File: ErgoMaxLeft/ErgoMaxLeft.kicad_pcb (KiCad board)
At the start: 2 copper layers, 182.8 x 178.9 mm, 94 parts, among them J1 AudioJack4_Ground, K1 KEYSW, K10 KEYSW, K11 KEYSW, K12 KEYSW, K13 KEYSW, K14 KEYSW, K15 KEYSW, K16 KEYSW, K17 KEYSW, K18 KEYSW, K19 KEYSW, K2 KEYSW, K20 KEYSW, K21 KEYSW, K22 KEYSW, K23 KEYSW, K24 KEYSW, K25 KEYSW, K26 KEYSW, K27 KEYSW, K28 KEYSW, K29 KEYSW, K3 KEYSW, K30 KEYSW, K31 KEYSW, K32 KEYSW, K33 KEYSW, K34 KEYSW, K35 KEYSW, K36 KEYSW, K37 KEYSW, K38 KEYSW, K39 KEYSW, K4 KEYSW, K40 KEYSW, K41 KEYSW, K42 KEYSW, K43 KEYSW, K44 KEYSW, K5 KEYSW, K6 KEYSW, K7 KEYSW, K8 KEYSW, K9 KEYSW, U1 ProMicro

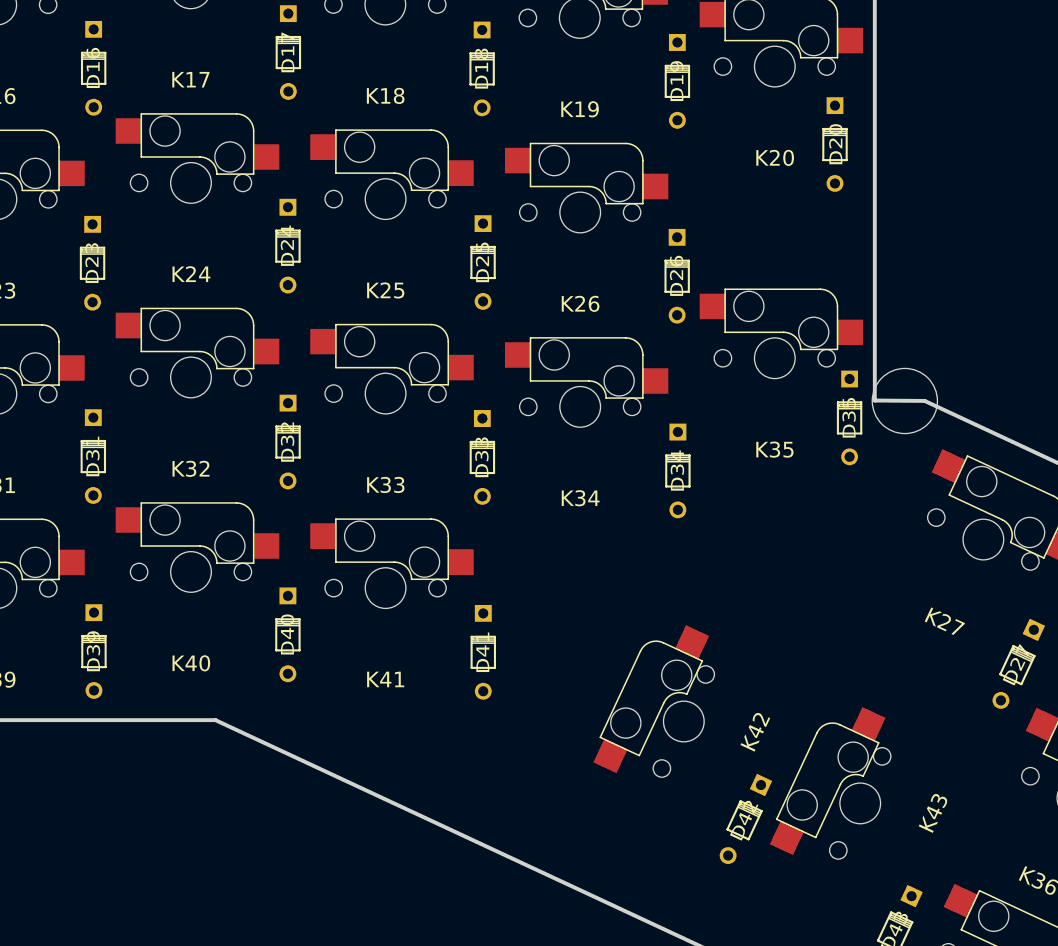
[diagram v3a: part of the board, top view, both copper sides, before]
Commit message: WIP PCB - add more mouting holes based on ErgoDox
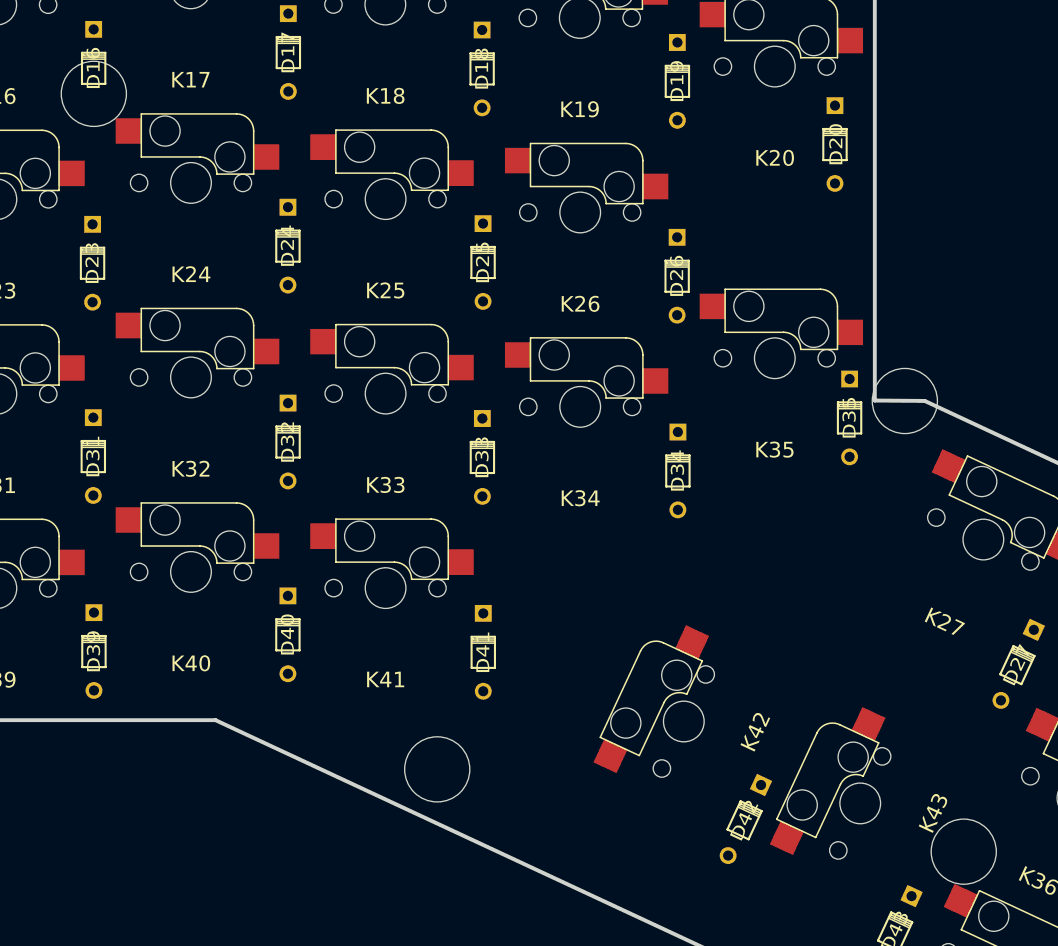
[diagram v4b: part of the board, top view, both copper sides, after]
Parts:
- added ?: , MountingHole:MountingHole_6.5mm_Pad, F.Cu at (177.2, 107.3)
- added ?: , MountingHole:MountingHole_6.5mm_Pad, F.Cu at (262.4, 181.5)
- added ?: , MountingHole:MountingHole_6.5mm_Pad, F.Cu at (210.8, 173.4)
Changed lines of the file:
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@@
     (tracks 0)
     (zones 0)
-    (modules 94)
+    (modules 97)
     (nets 67)
   )
@@
     (add_net VCC)
   )
+  (module MountingHole:MountingHole_6.5mm_Pad (layer F.Cu)
+    (at 177.200212 107.268092)
+    (descr "Mounting Hole 6.5mm")
+    (tags "mounting hole 6.5mm")
+    (attr virtual)
+    (fp_text reference "" (at 0 -7.5) (layer F.SilkS) hide
+      (effects (font (size 1 1) (thickness 0.15)))
+    )
+    (fp_text value "" (at 0 7.5) (layer F.Fab) hide
+      (effects (font (size 1 1) (thickness 0.15)))
+    )
+    (fp_text user %R (at 0.3 0) (layer F.Fab)
+      (effects (font (size 1 1) (thickness 0.15)))
+    )
+    (fp_circle (center 0 0) (end 6.5 0) (layer Cmts.User) (width 0.15))
+    (fp_circle (center 0 0) (end 6.75 0) (layer F.CrtYd) (width 0.05))
+    (pad "" np_thru_hole circle (at 0 0) (size 6.3754 6.3754) (drill 6.3754) (layers *.Cu *.Mask)
+      (solder_mask_margin -0.254))
+  )
+  (module MountingHole:MountingHole_6.5mm_Pad (layer F.Cu)
+    (at 262.355601 181.45146)
+    (descr "Mounting Hole 6.5mm")
+    (tags "mounting hole 6.5mm")
+    (attr virtual)
+    (fp_text reference "" (at 0 -7.5) (layer F.SilkS) hide
+      (effects (font (size 1 1) (thickness 0.15)))
+    )
+    (fp_text value "" (at 0 7.5) (layer F.Fab) hide
+      (effects (font (size 1 1) (thickness 0.15)))
+    )
+    (fp_text user %R (at 0.3 0) (layer F.Fab)
+      (effects (font (size 1 1) (thickness 0.15)))
+    )
+    (fp_circle (center 0 0) (end 6.5 0) (layer Cmts.User) (width 0.15))
+    (fp_circle (center 0 0) (end 6.75 0) (layer F.CrtYd) (width 0.05))
+    (pad "" np_thru_hole circle (at 0 0) (size 6.3754 6.3754) (drill 6.3754) (layers *.Cu *.Mask)
+      (solder_mask_margin -0.254))
+  )
+  (module MountingHole:MountingHole_6.5mm_Pad (layer F.Cu)
+    (at 210.814547 173.394127)
+    (descr "Mounting Hole 6.5mm")
+    (tags "mounting hole 6.5mm")
+    (attr virtual)
+    (fp_text reference "" (at 0 -7.5) (layer F.SilkS) hide
+      (effects (font (size 1 1) (thickness 0.15)))
+    )
+    (fp_text value "" (at 0 7.5) (layer F.Fab) hide
+      (effects (font (size 1 1) (thickness 0.15)))
+    )
+    (fp_text user %R (at 0.3 0) (layer F.Fab)
+      (effects (font (size 1 1) (thickness 0.15)))
+    )
+    (fp_circle (center 0 0) (end 6.5 0) (layer Cmts.User) (width 0.15))
+    (fp_circle (center 0 0) (end 6.75 0) (layer F.CrtYd) (width 0.05))
+    (pad "" np_thru_hole circle (at 0 0) (size 6.3754 6.3754) (drill 6.3754) (layers *.Cu *.Mask)
+      (solder_mask_margin -0.254))
+  )
   (module MountingHole:MountingHole_6.4mm_M6 (layer F.Cu)

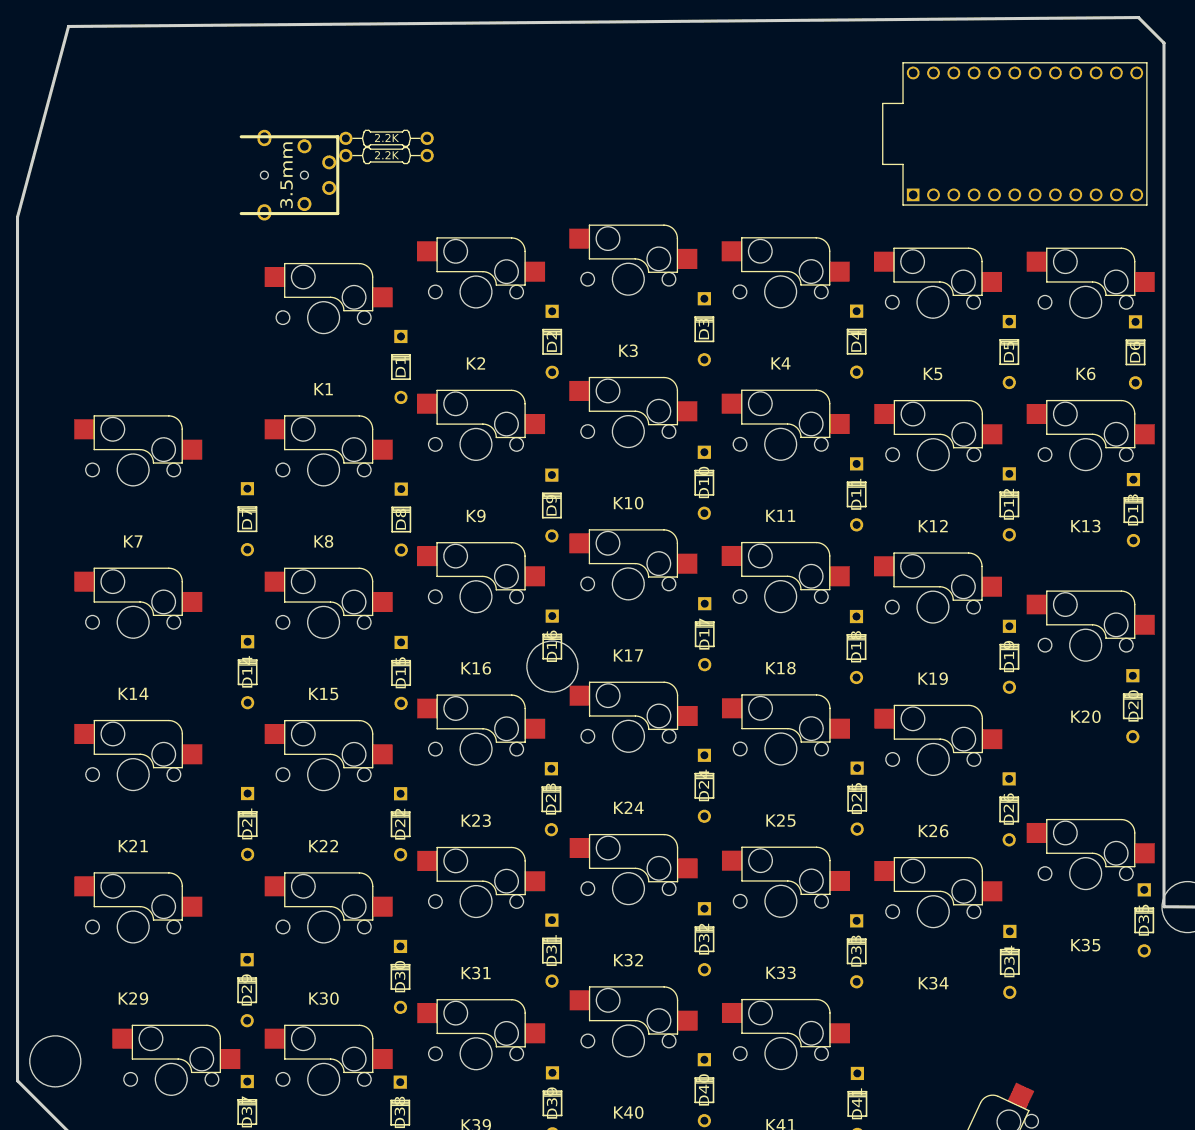
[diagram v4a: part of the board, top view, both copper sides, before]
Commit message: WIP PCB - make proper cutout for the top
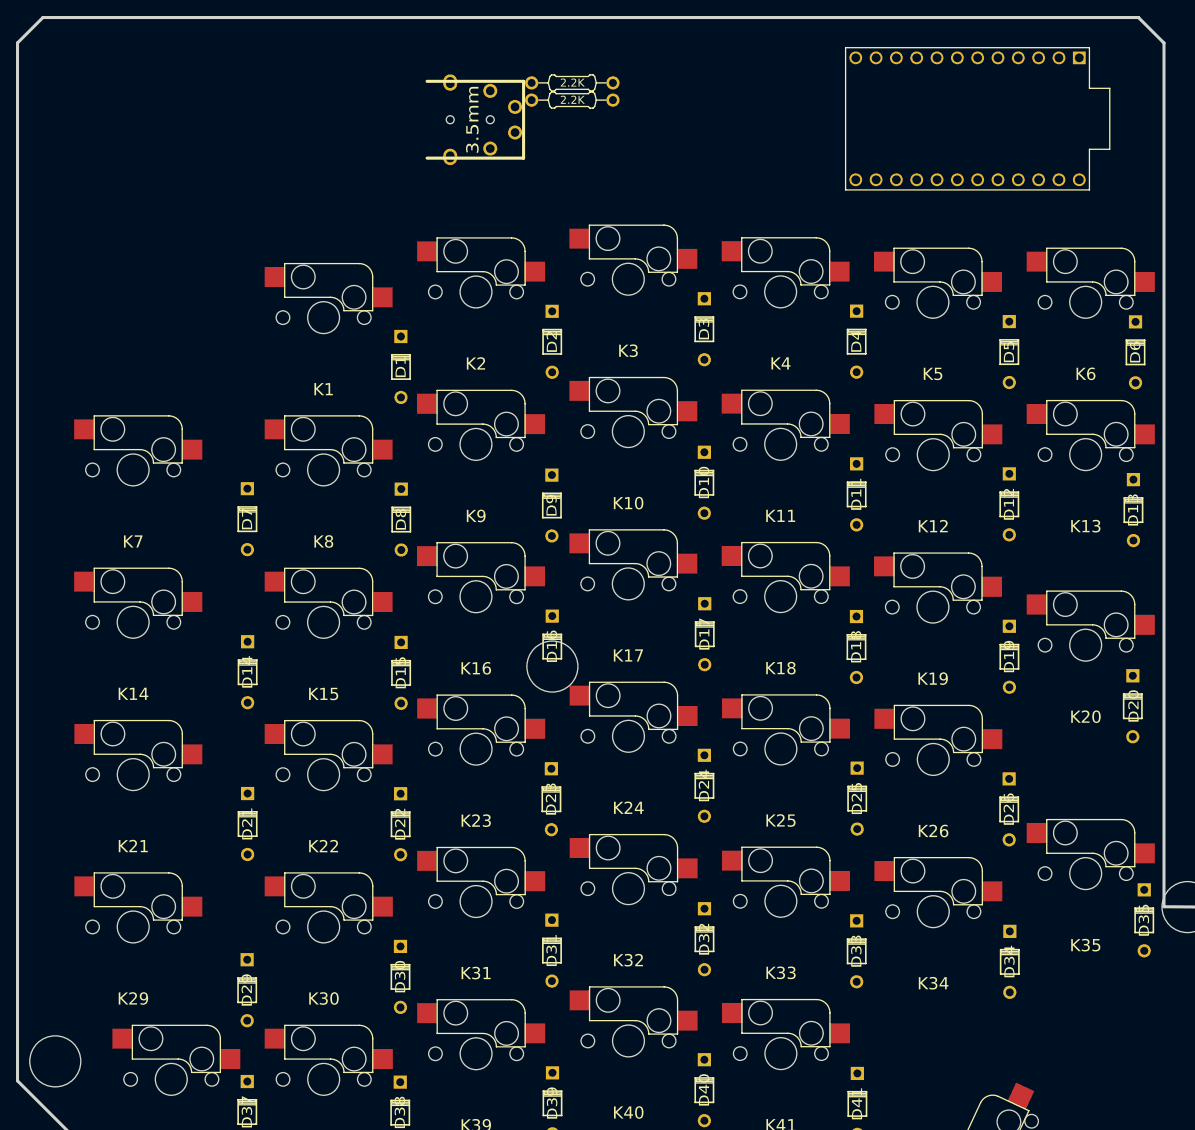
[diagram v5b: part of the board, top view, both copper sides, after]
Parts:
- moved J1 24.2 mm to (161.5, 38.9)
- moved R1 24.2 mm to (179.7, 36.5)
- moved R2 24.2 mm to (179.7, 34.3)
- moved U1 7.42 mm to (229.1, 38.8), turned to 180 degrees
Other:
- outline, holes or cut-outs redrawn
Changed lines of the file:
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@@
   )
   (module Keebio-Parts:4pin35mmAudio (layer F.Cu)
-    (at 138.30298 45.84516)
+    (at 161.53298 38.91516)
     (fp_text reference J1 (at 1.27 0 90) (layer F.SilkS) hide
       (effects (font (size 1.524 1.778) (thickness 0.3048)))
@@
   )
   (module Keebio-Parts:Resistor (layer F.Cu)
-    (at 156.45848 43.393261)
+    (at 179.68848 36.463261)
     (fp_text reference R1 (at 0 0) (layer F.SilkS) hide
       (effects (font (size 1 1) (thickness 0.2)))
@@
   )
   (module Keebio-Parts:Resistor (layer F.Cu)
-    (at 156.45848 41.243261)
+    (at 179.68848 34.313261)
     (fp_text reference R2 (at 0 0) (layer F.SilkS) hide
       (effects (font (size 1 1) (thickness 0.2)))
@@
   )
   (module promicro:ProMicro (layer F.Cu)
-    (at 236.27 40.69)
+    (at 229.09 38.8 180)
     (descr "Pro Micro footprint")
     (tags "promicro ProMicro")
-    (fp_text reference U1 (at 0 -10.16) (layer F.SilkS) hide
+    (fp_text reference U1 (at 0 -10.16 180) (layer F.SilkS) hide
       (effects (font (size 1 1) (thickness 0.15)))
     )
-    (fp_text value ProMicro (at 0 10.16) (layer F.Fab)
+    (fp_text value ProMicro (at 0 10.16 180) (layer F.Fab)
       (effects (font (size 1 1) (thickness 0.15)))
     )
@@
     (fp_line (start 15.24 8.89) (end -15.24 8.89) (layer B.SilkS) (width 0.15))
     (fp_line (start 15.24 -8.89) (end 15.24 8.89) (layer B.SilkS) (width 0.15))
-    (pad 24 thru_hole circle (at -13.97 -7.62) (size 1.6 1.6) (drill 1.1) (layers *.Cu *.Mask F.SilkS)
+    (pad 24 thru_hole circle (at -13.97 -7.62 180) (size 1.6 1.6) (drill 1.1) (layers *.Cu *.Mask F.SilkS)
       (net 66 "Net-(U1-Pad24)"))
-    (pad 23 thru_hole circle (at -11.43 -7.62) (size 1.6 1.6) (drill 1.1) (layers *.Cu *.Mask F.SilkS)
+    (pad 23 thru_hole circle (at -11.43 -7.62 180) (size 1.6 1.6) (drill 1.1) (layers *.Cu *.Mask F.SilkS)
       (net 64 GND))
-    (pad 22 thru_hole circle (at -8.89 -7.62) (size 1.6 1.6) (drill 1.1) (layers *.Cu *.Mask F.SilkS)
+    (pad 22 thru_hole circle (at -8.89 -7.62 180) (size 1.6 1.6) (drill 1.1) (layers *.Cu *.Mask F.SilkS)
       (net 65 "Net-(U1-Pad22)"))
-    (pad 21 thru_hole circle (at -6.35 -7.62) (size 1.6 1.6) (drill 1.1) (layers *.Cu *.Mask F.SilkS)
+    (pad 21 thru_hole circle (at -6.35 -7.62 180) (size 1.6 1.6) (drill 1.1) (layers *.Cu *.Mask F.SilkS)
       (net 59 VCC))
-    (pad 20 thru_hole circle (at -3.81 -7.62) (size 1.6 1.6) (drill 1.1) (layers *.Cu *.Mask F.SilkS)
+    (pad 20 thru_hole circle (at -3.81 -7.62 180) (size 1.6 1.6) (drill 1.1) (layers *.Cu *.Mask F.SilkS)
       (net 13 /Col0))
-    (pad 19 thru_hole circle (at -1.27 -7.62) (size 1.6 1.6) (drill 1.1) (layers *.Cu *.Mask F.SilkS)
+    (pad 19 thru_hole circle (at -1.27 -7.62 180) (size 1.6 1.6) (drill 1.1) (layers *.Cu *.Mask F.SilkS)
       (net 2 /Col1))
-    (pad 18 thru_hole circle (at 1.27 -7.62) (size 1.6 1.6) (drill 1.1) (layers *.Cu *.Mask F.SilkS)
+    (pad 18 thru_hole circle (at 1.27 -7.62 180) (size 1.6 1.6) (drill 1.1) (layers *.Cu *.Mask F.SilkS)
       (net 4 /Col2))
-    (pad 17 thru_hole circle (at 3.81 -7.62) (size 1.6 1.6) (drill 1.1) (layers *.Cu *.Mask F.SilkS)
+    (pad 17 thru_hole circle (at 3.81 -7.62 180) (size 1.6 1.6) (drill 1.1) (layers *.Cu *.Mask F.SilkS)
       (net 5 /Col3))
-    (pad 16 thru_hole circle (at 6.35 -7.62) (size 1.6 1.6) (drill 1.1) (layers *.Cu *.Mask F.SilkS)
+    (pad 16 thru_hole circle (at 6.35 -7.62 180) (size 1.6 1.6) (drill 1.1) (layers *.Cu *.Mask F.SilkS)
       (net 8 /Col4))
-    (pad 15 thru_hole circle (at 8.89 -7.62) (size 1.6 1.6) (drill 1.1) (layers *.Cu *.Mask F.SilkS)
+    (pad 15 thru_hole circle (at 8.89 -7.62 180) (size 1.6 1.6) (drill 1.1) (layers *.Cu *.Mask F.SilkS)
       (net 10 /Col5))
-    (pad 14 thru_hole circle (at 11.43 -7.62) (size 1.6 1.6) (drill 1.1) (layers *.Cu *.Mask F.SilkS)
+    (pad 14 thru_hole circle (at 11.43 -7.62 180) (size 1.6 1.6) (drill 1.1) (layers *.Cu *.Mask F.SilkS)
       (net 11 /Col6))
-    (pad 13 thru_hole circle (at 13.97 -7.62) (size 1.6 1.6) (drill 1.1) (layers *.Cu *.Mask F.SilkS)
+    (pad 13 thru_hole circle (at 13.97 -7.62 180) (size 1.6 1.6) (drill 1.1) (layers *.Cu *.Mask F.SilkS)
       (net 35 /Col7))
-    (pad 12 thru_hole circle (at 13.97 7.62) (size 1.6 1.6) (drill 1.1) (layers *.Cu *.Mask F.SilkS)
+    (pad 12 thru_hole circle (at 13.97 7.62 180) (size 1.6 1.6) (drill 1.1) (layers *.Cu *.Mask F.SilkS)
       (net 58 /Row5))
-    (pad 11 thru_hole circle (at 11.43 7.62) (size 1.6 1.6) (drill 1.1) (layers *.Cu *.Mask F.SilkS)
+    (pad 11 thru_hole circle (at 11.43 7.62 180) (size 1.6 1.6) (drill 1.1) (layers *.Cu *.Mask F.SilkS)
       (net 57 /Row4))
-    (pad 10 thru_hole circle (at 8.89 7.62) (size 1.6 1.6) (drill 1.1) (layers *.Cu *.Mask F.SilkS)
+    (pad 10 thru_hole circle (at 8.89 7.62 180) (size 1.6 1.6) (drill 1.1) (layers *.Cu *.Mask F.SilkS)
       (net 56 /Row3))
-    (pad 9 thru_hole circle (at 6.35 7.62) (size 1.6 1.6) (drill 1.1) (layers *.Cu *.Mask F.SilkS)
+    (pad 9 thru_hole circle (at 6.35 7.62 180) (size 1.6 1.6) (drill 1.1) (layers *.Cu *.Mask F.SilkS)
       (net 55 /Row2))
-    (pad 8 thru_hole circle (at 3.81 7.62) (size 1.6 1.6) (drill 1.1) (layers *.Cu *.Mask F.SilkS)
+    (pad 8 thru_hole circle (at 3.81 7.62 180) (size 1.6 1.6) (drill 1.1) (layers *.Cu *.Mask F.SilkS)
       (net 54 /Row1))
-    (pad 7 thru_hole circle (at 1.27 7.62) (size 1.6 1.6) (drill 1.1) (layers *.Cu *.Mask F.SilkS)
+    (pad 7 thru_hole circle (at 1.27 7.62 180) (size 1.6 1.6) (drill 1.1) (layers *.Cu *.Mask F.SilkS)
       (net 53 /Row0))
-    (pad 6 thru_hole circle (at -1.27 7.62) (size 1.6 1.6) (drill 1.1) (layers *.Cu *.Mask F.SilkS)
+    (pad 6 thru_hole circle (at -1.27 7.62 180) (size 1.6 1.6) (drill 1.1) (layers *.Cu *.Mask F.SilkS)
       (net 61 SCL))
-    (pad 5 thru_hole circle (at -3.81 7.62) (size 1.6 1.6) (drill 1.1) (layers *.Cu *.Mask F.SilkS)
+    (pad 5 thru_hole circle (at -3.81 7.62 180) (size 1.6 1.6) (drill 1.1) (layers *.Cu *.Mask F.SilkS)
       (net 60 SDA))
-    (pad 4 thru_hole circle (at -6.35 7.62) (size 1.6 1.6) (drill 1.1) (layers *.Cu *.Mask F.SilkS)
+    (pad 4 thru_hole circle (at -6.35 7.62 180) (size 1.6 1.6) (drill 1.1) (layers *.Cu *.Mask F.SilkS)
       (net 64 GND))
-    (pad 3 thru_hole circle (at -8.89 7.62) (size 1.6 1.6) (drill 1.1) (layers *.Cu *.Mask F.SilkS)
+    (pad 3 thru_hole circle (at -8.89 7.62 180) (size 1.6 1.6) (drill 1.1) (layers *.Cu *.Mask F.SilkS)
       (net 64 GND))
-    (pad 2 thru_hole circle (at -11.43 7.62) (size 1.6 1.6) (drill 1.1) (layers *.Cu *.Mask F.SilkS)
+    (pad 2 thru_hole circle (at -11.43 7.62 180) (size 1.6 1.6) (drill 1.1) (layers *.Cu *.Mask F.SilkS)
       (net 63 "Net-(U1-Pad2)"))
-    (pad 1 thru_hole rect (at -13.97 7.62) (size 1.6 1.6) (drill 1.1) (layers *.Cu *.Mask F.SilkS)
+    (pad 1 thru_hole rect (at -13.97 7.62 180) (size 1.6 1.6) (drill 1.1) (layers *.Cu *.Mask F.SilkS)
       (net 62 "Net-(U1-Pad1)"))
   )
@@
       (solder_mask_margin -0.254))
   )
+  (gr_line (start 113.515 26.14) (end 110.34 29.315) (layer Edge.Cuts) (width 0.381))
   (gr_line (start 253.65 137.29) (end 258.55 137.33) (layer Edge.Cuts) (width 0.381))
-  (gr_line (start 116.72 27.25) (end 110.34 51.1) (layer Edge.Cuts) (width 0.381))
-  (gr_line (start 250.48 26.14) (end 116.72 27.26) (layer Edge.Cuts) (width 0.381))
+  (gr_line (start 250.48 26.14) (end 113.514 26.14) (layer Edge.Cuts) (width 0.381))
   (gr_line (start 253.65 29.33) (end 250.475 26.155) (layer Edge.Cuts) (width 0.381))
   (gr_line (start 253.65 29.34) (end 253.65 137.29) (layer Edge.Cuts) (width 0.381))
@@
   (gr_line (start 189.105 168.575) (end 267.2735 205.01892) (layer Edge.Cuts) (width 0.381))
   (gr_line (start 119.865 168.575) (end 189.105 168.575) (layer Edge.Cuts) (width 0.381))
-  (gr_line (start 110.34 51.1) (end 110.34 159.05) (layer Edge.Cuts) (width 0.381))
+  (gr_line (start 110.34 29.315) (end 110.34 159.05) (layer Edge.Cuts) (width 0.381))
 )
